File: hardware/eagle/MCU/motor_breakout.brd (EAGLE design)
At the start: 100 x 80 mm, 17 parts, among them X1 1751248, X2 1751248

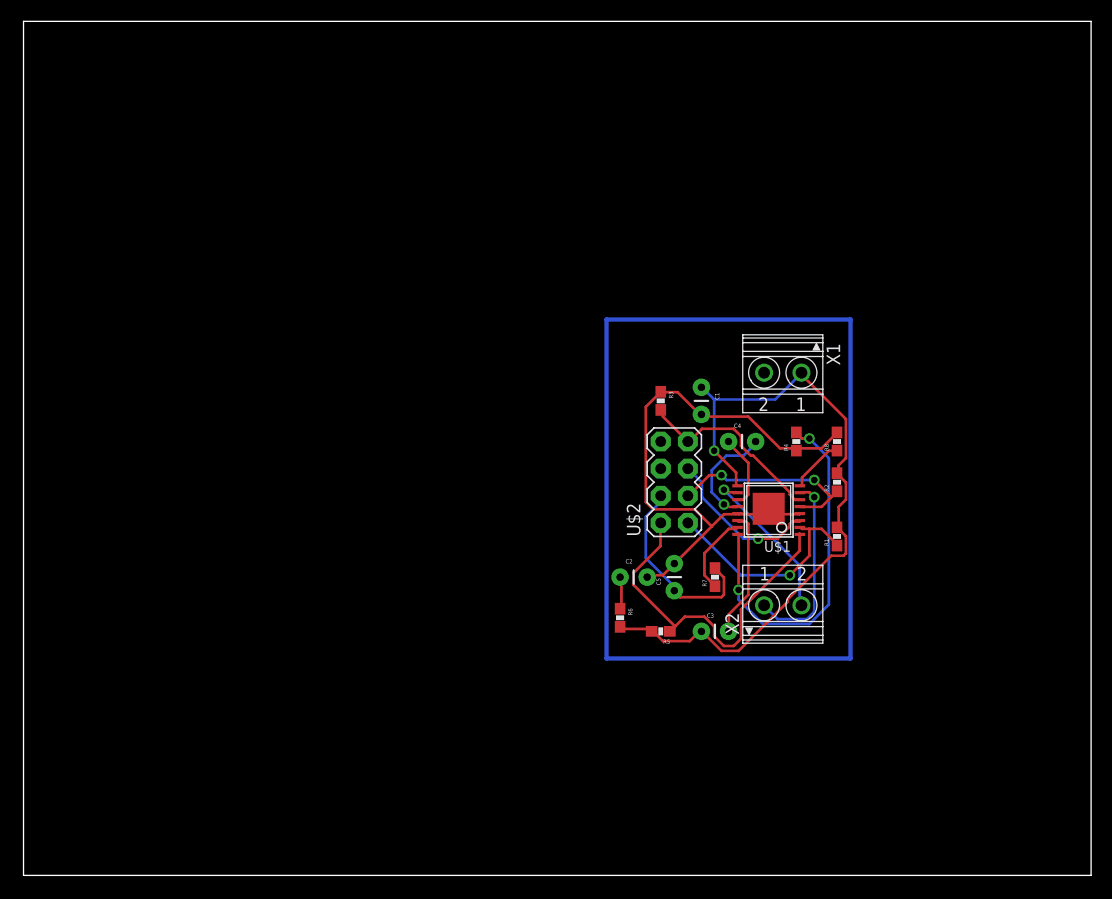
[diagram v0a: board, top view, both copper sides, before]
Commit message: added ground pour and power connection to MCU breakout
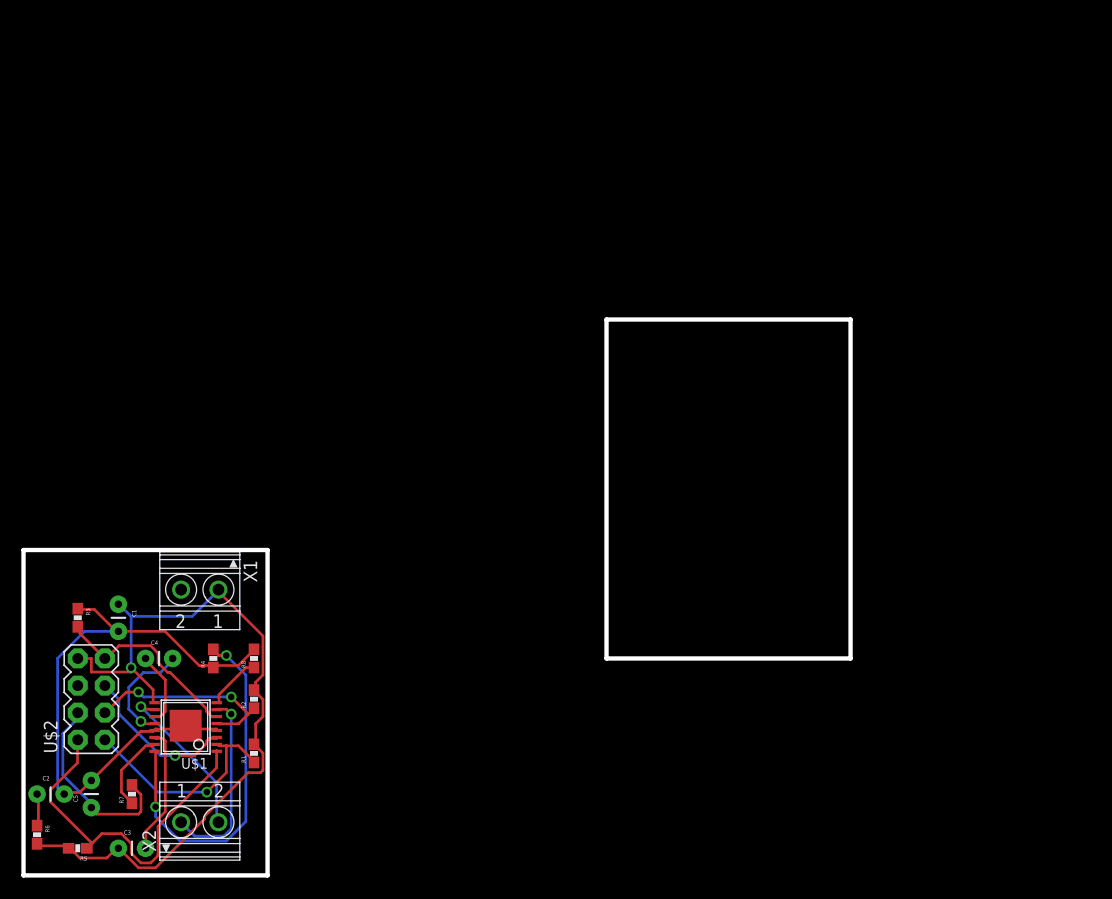
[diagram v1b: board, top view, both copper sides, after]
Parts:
- moved C4 58.3 mm to (11.4, 20.3)
- moved C1 58.3 mm to (8.89, 25.4)
- moved C2 58.3 mm to (1.27, 7.62)
- moved C3 58.3 mm to (8.89, 2.54)
- moved C5 58.3 mm to (6.35, 6.35)
- moved R1 58.3 mm to (21.6, 11.4)
- moved R2 58.3 mm to (21.6, 16.5)
- moved R3 58.3 mm to (5.08, 24.1)
- moved R4 58.3 mm to (17.8, 20.3)
- moved R5 58.3 mm to (5.08, 2.54)
- moved R6 58.3 mm to (1.27, 3.81)
- moved R7 58.3 mm to (10.2, 7.62)
- moved R8 58.3 mm to (21.6, 20.3)
- moved U$2 58.3 mm to (6.35, 16.5)
- moved X1 58.3 mm to (16.5, 26.7)
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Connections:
- removed net N$10: U$2.8
- net VDD: now also U$2.8
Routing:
- net N$3: track 109.2 -> 0.00 mm
- net VDD: track 66.8 -> 73.5 mm
- net GND: track 54.9 -> 56.5 mm
- added copper zone on layer 1, net GND
- added copper zone on layer 16, net GND
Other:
- board size 100 x 80 mm -> 77.5 x 52.1 mm

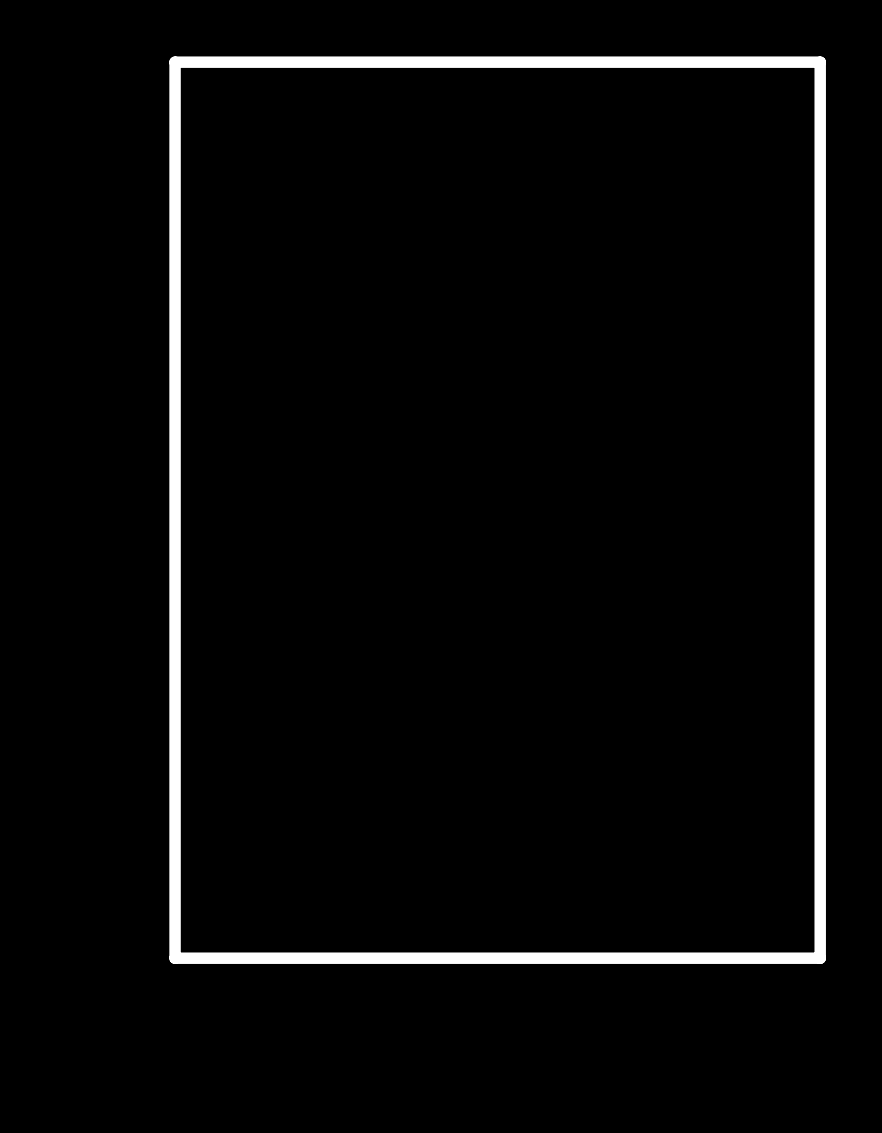
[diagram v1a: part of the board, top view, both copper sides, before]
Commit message: started breakout board connecting arduino pins to components
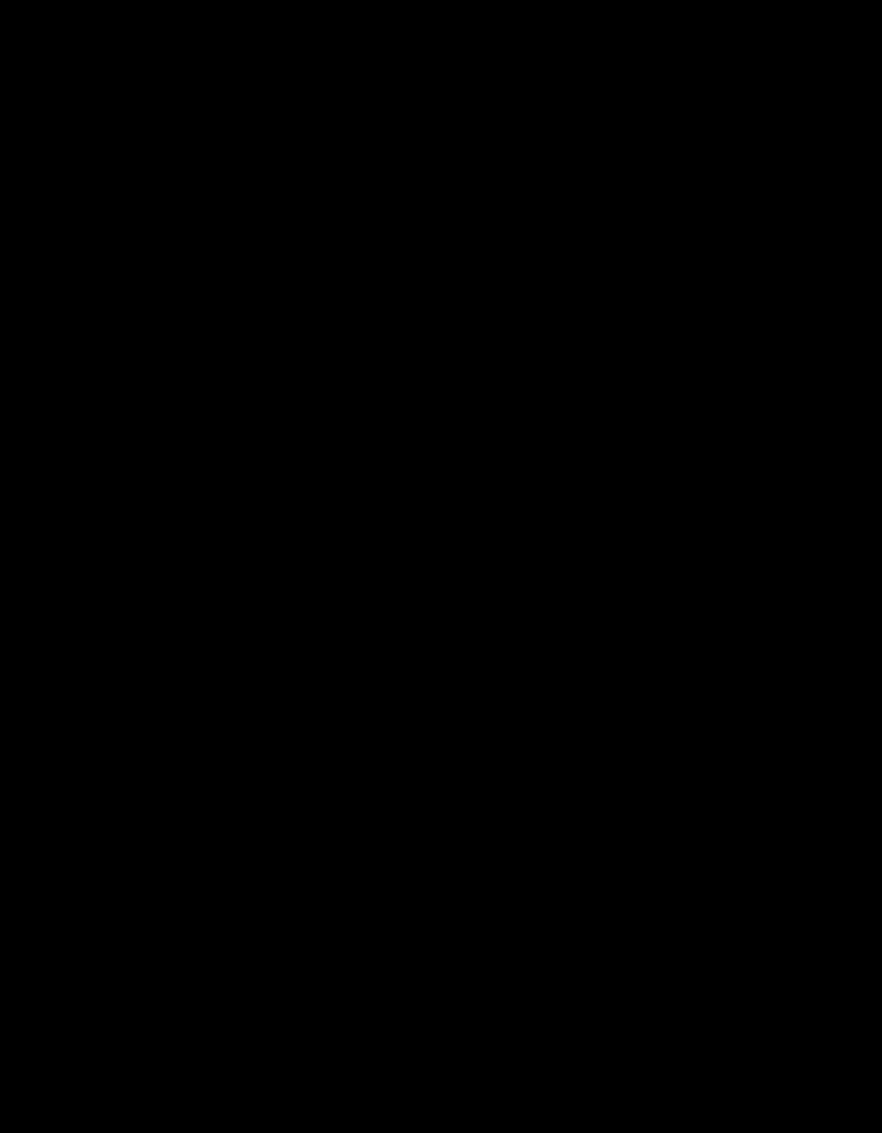
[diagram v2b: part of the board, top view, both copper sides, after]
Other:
- board size 77.5 x 52.1 mm -> 22.9 x 30.5 mm
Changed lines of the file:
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@@
 <board>
 <plain>
-<wire x1="54.61" y1="52.07" x2="54.61" y2="20.32" width="0.4064" layer="20"/>
-<wire x1="54.61" y1="20.32" x2="77.47" y2="20.32" width="0.4064" layer="20"/>
-<wire x1="77.47" y1="20.32" x2="77.47" y2="52.07" width="0.4064" layer="20"/>
-<wire x1="77.47" y1="52.07" x2="54.61" y2="52.07" width="0.4064" layer="20"/>
 <wire x1="0" y1="0" x2="0" y2="30.48" width="0.4064" layer="20"/>
 <wire x1="0" y1="30.48" x2="22.86" y2="30.48" width="0.4064" layer="20"/>
